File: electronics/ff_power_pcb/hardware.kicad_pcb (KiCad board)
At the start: 4 copper layers, 60 x 37 mm, 60 parts, among them J1 Conn_01x01_Female, J2 Conn_01x01_Female, J3 Conn_01x07_Male, U3 TPS62095RGTR, U4 TPS62095RGTR, U5 TPS62095RGTR, U6 TPS62095RGTR, U7 AP131-25

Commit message: Generated gerbers for R0.1 power board.
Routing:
- net +5V: track 53.3 -> 53.8 mm
- net GND: vias 42 -> 46
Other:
- board text added: "Ryan Walker Interrupt Labs WifiWart - Power Board R0.1"

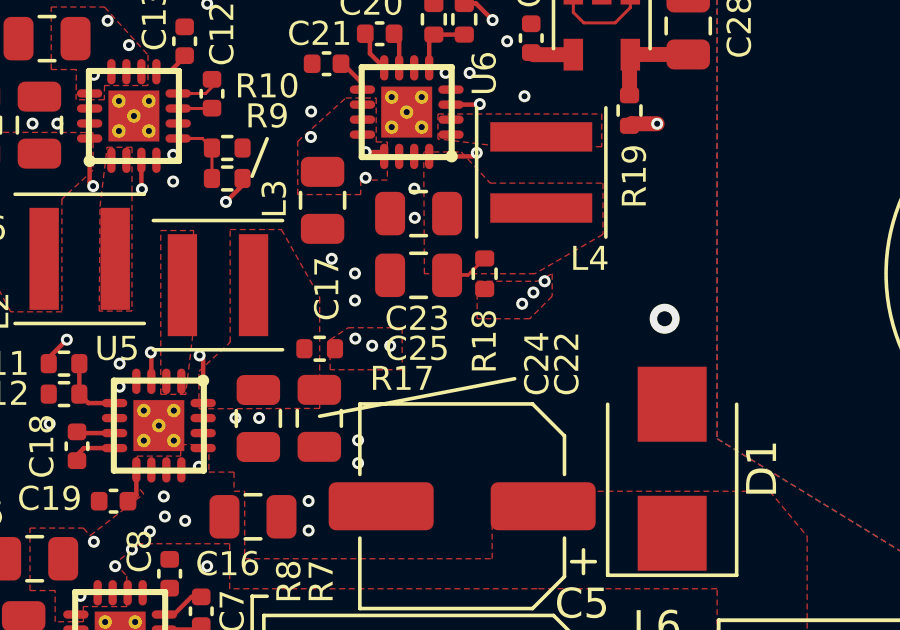
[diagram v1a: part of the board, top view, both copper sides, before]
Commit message: Rerouted the power traces for R0.1 power pcb - they didn't match the compute PCB power pins.
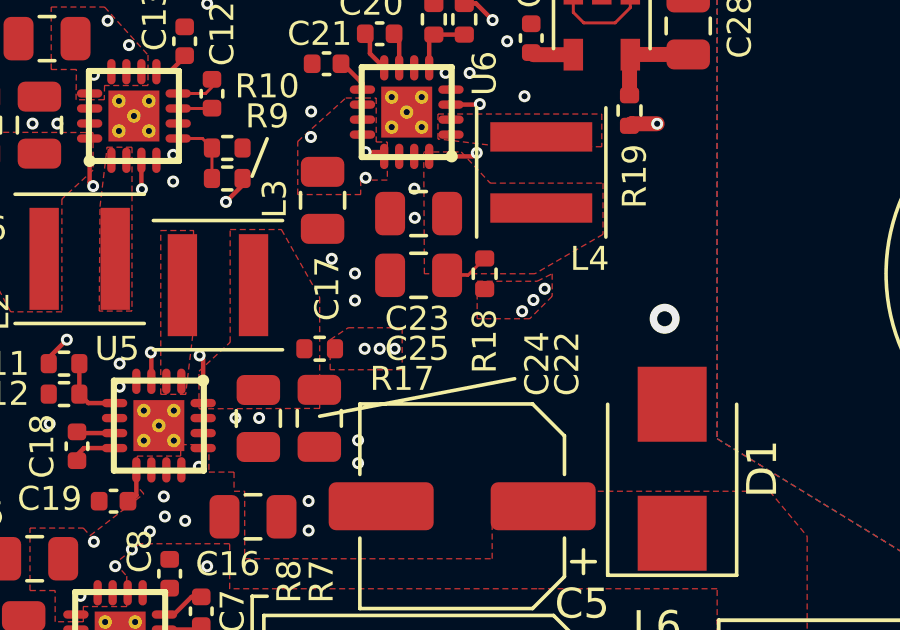
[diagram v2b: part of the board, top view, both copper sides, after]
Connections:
- J3 pad 5: +2V5 -> +1V1
- J3 pad 6: +1V35 -> +2V5
- J3 pad 7: +1V1 -> +1V35
- U3 pad 4: Net-(U3-Pad4) -> (no net)
- U4 pad 4: Net-(U4-Pad4) -> (no net)
- U5 pad 4: Net-(U5-Pad4) -> (no net)
- U6 pad 4: Net-(U6-Pad4) -> (no net)
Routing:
- net +1V1: track 13.5 -> 24.6 mm
- net +2V5: track 16.7 -> 14.6 mm
- net +1V35: track 16.5 -> 18.3 mm
